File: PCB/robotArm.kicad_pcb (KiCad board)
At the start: 2 copper layers, 66 parts, among them J1 Motor_eje_X, J10 Gripper, J11 Conector Auxiliar 2, J12 5v, J13 End-Stop-X, J14 End-Stop-Y, J15 End-Stop-Z, J16 jumperLed5v, J17 Conector Auxiliar 1, J18 jumperLedVbat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

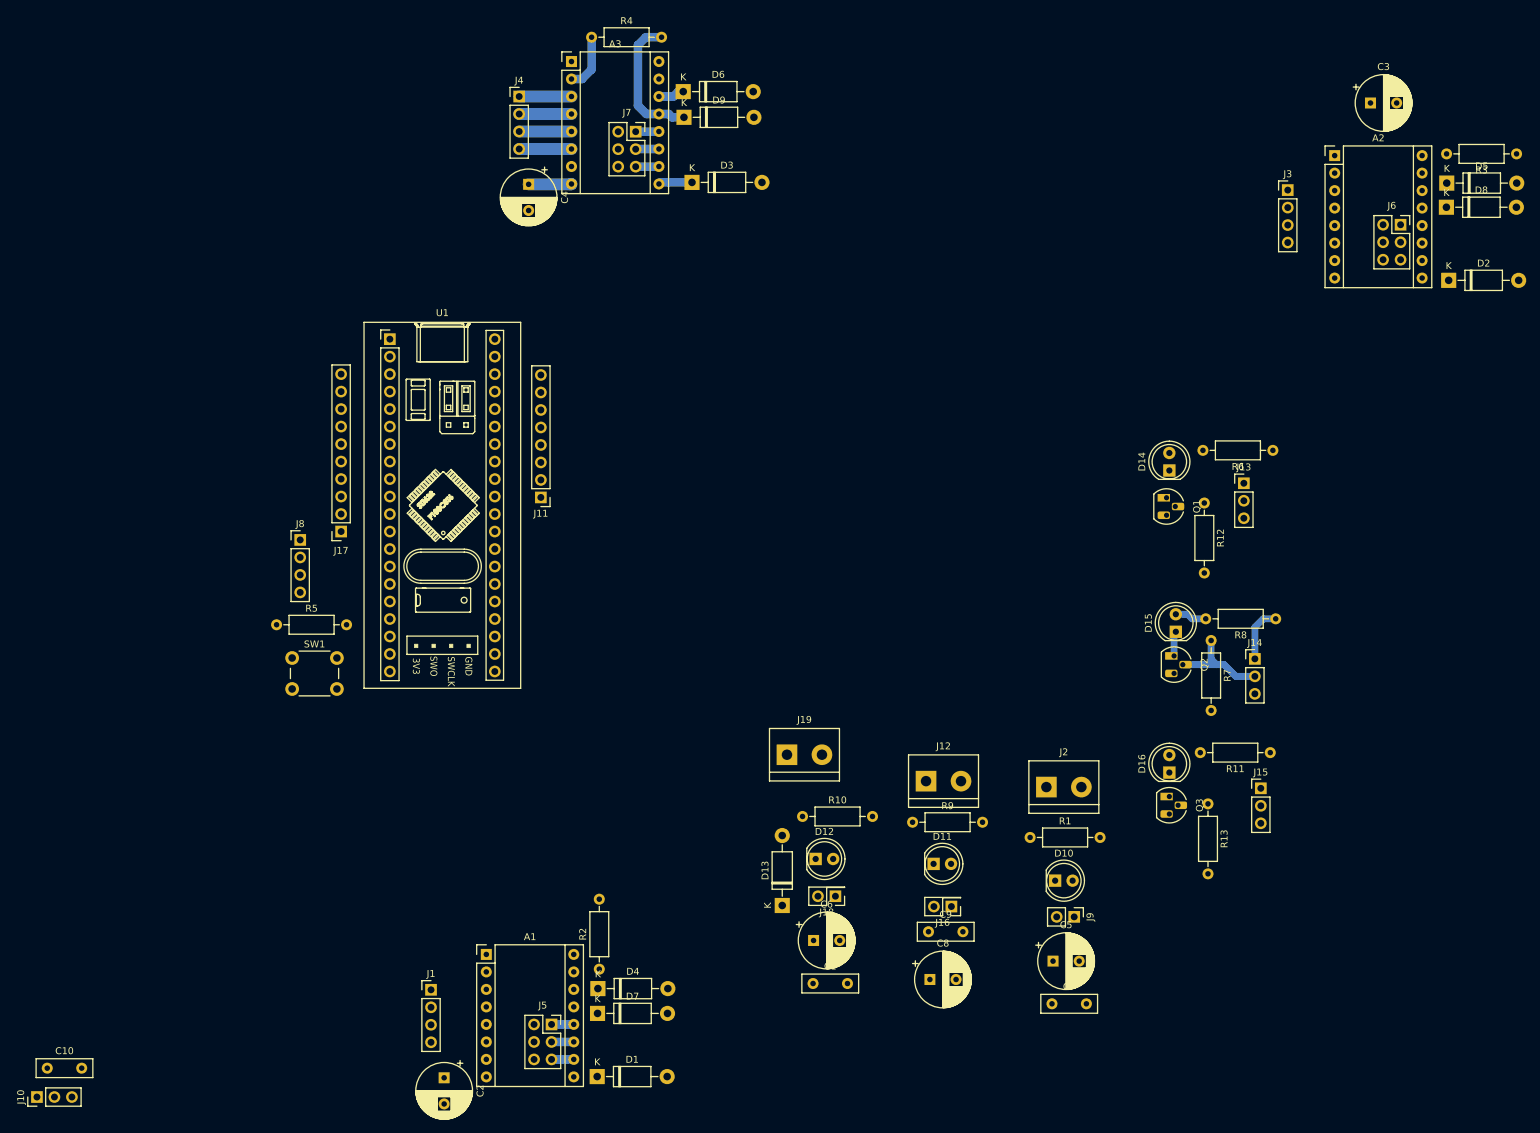
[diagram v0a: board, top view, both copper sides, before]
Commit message: Se avanzó con el diseño de la PCB, falta resolver Vin
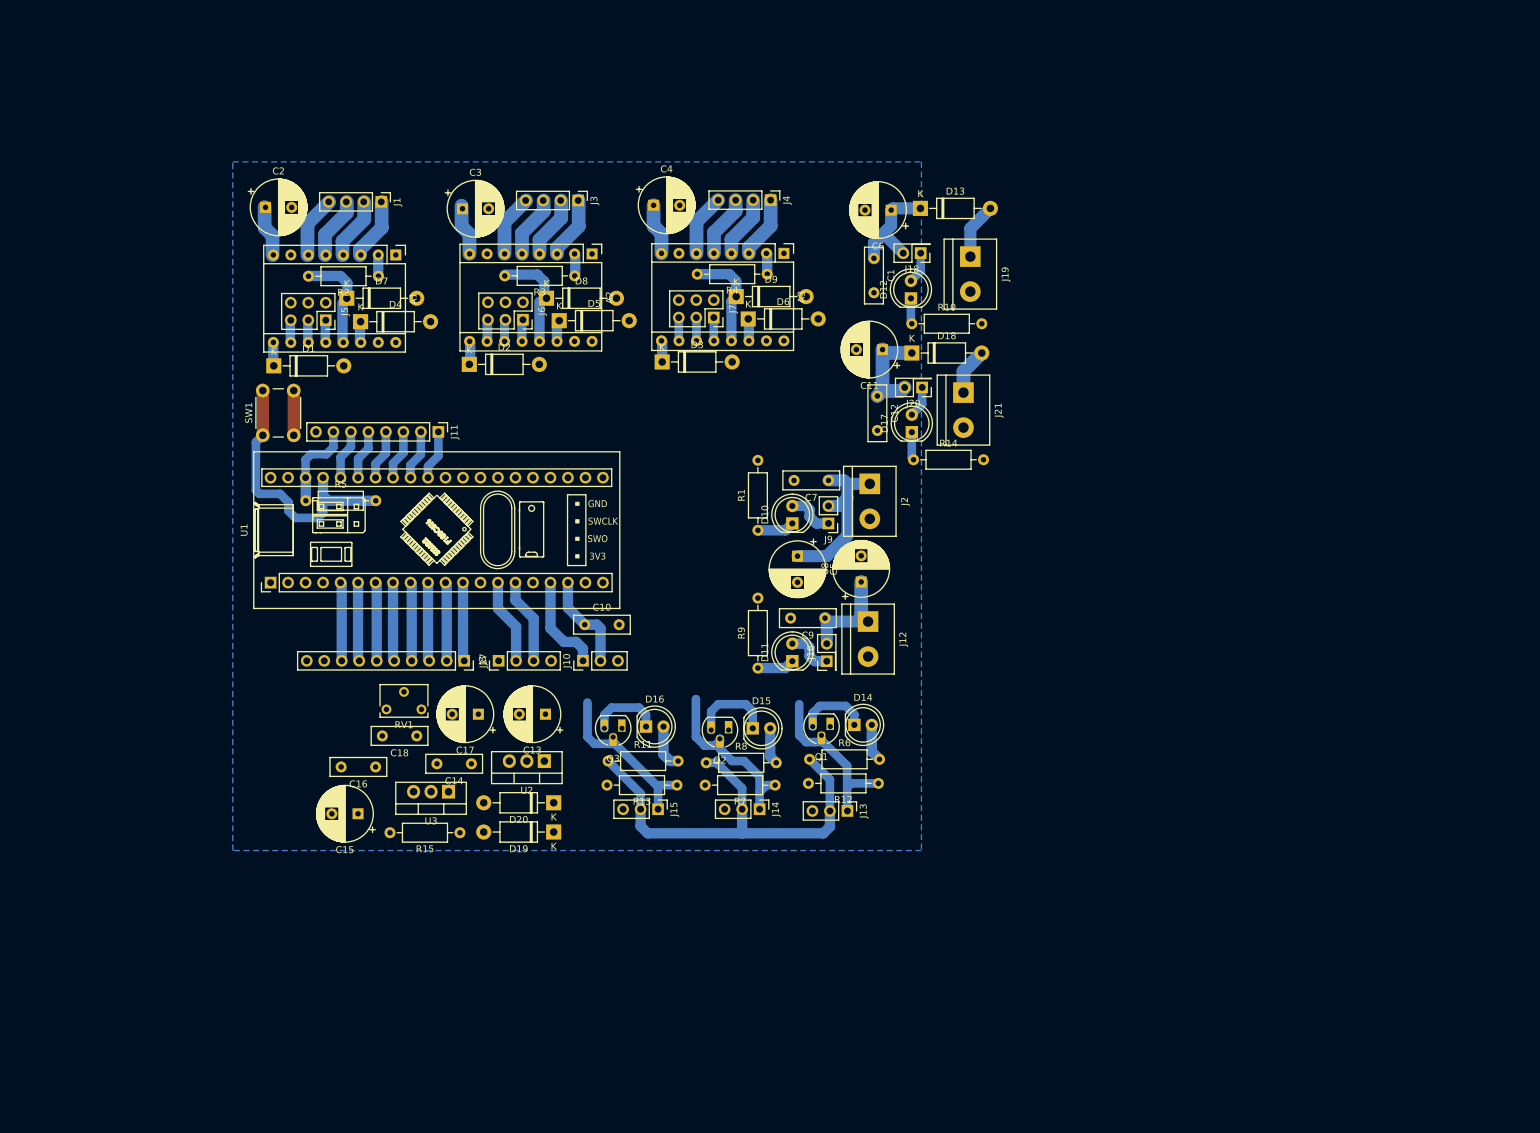
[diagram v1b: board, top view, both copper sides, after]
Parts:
- added C11: 470uF, Capacitor_THT:CP_Radial_D8.0mm_P3.80mm, F.Cu at (153.4, 76.7)
- added C12: 103, Capacitor_THT:C_Disc_D8.0mm_W2.5mm_P5.00mm, F.Cu at (152.7, 83.4)
- added C13: 470uF, Capacitor_THT:CP_Radial_D8.0mm_P3.80mm, F.Cu at (104.5, 129.6)
- added C14: 103, Capacitor_THT:C_Disc_D8.0mm_W2.5mm_P5.00mm, F.Cu at (93.7, 136.8)
- added C15: 220uF, Capacitor_THT:CP_Radial_D8.0mm_P3.80mm, F.Cu at (77.2, 144.1)
- added C16: 104, Capacitor_THT:C_Disc_D8.0mm_W2.5mm_P5.00mm, F.Cu at (79.8, 137.3)
- added C17: 100uF, Capacitor_THT:CP_Radial_D8.0mm_P3.80mm, F.Cu at (94.7, 129.6)
- added C18: 103, Capacitor_THT:C_Disc_D8.0mm_W2.5mm_P5.00mm, F.Cu at (85.8, 132.8)
- added D17: LED_Vcc, LED_THT:LED_D5.0mm, F.Cu at (157.7, 88.7)
- added D18: 1N4007, Diode_THT:D_DO-41_SOD81_P10.16mm_Horizontal, F.Cu at (157.7, 77.2)
- added D19: 1N4007, Diode_THT:D_DO-41_SOD81_P10.16mm_Horizontal, F.Cu at (105.6, 146.7)
- added D20: 1N4007, Diode_THT:D_DO-41_SOD81_P10.16mm_Horizontal, F.Cu at (105.6, 142.5)
- added J20: jumperLedVcc, Connector_PinHeader_2.54mm:PinHeader_2x01_P2.54mm_Vertical, F.Cu at (159.2, 82.2)
- added J21: Vcc, TerminalBlock:TerminalBlock_bornier-2_P5.08mm, F.Cu at (165.2, 82.9)
- added R14: 220, Resistor_THT:R_Axial_DIN0207_L6.3mm_D2.5mm_P10.16mm_Horizontal, F.Cu at (157.9, 92.7)
- added R15: 330, Resistor_THT:R_Axial_DIN0207_L6.3mm_D2.5mm_P10.16mm_Horizontal, F.Cu at (92.0, 146.8)
- added RV1: 1K, Potentiometer_THT:Potentiometer_Bourns_3266W_Vertical, F.Cu at (81.4, 128.9)
- added U2: LM7805_TO220, Package_TO_SOT_THT:TO-220-3_Vertical, F.Cu at (104.3, 136.4)
- added U3: LM317_TO-220, Package_TO_SOT_THT:TO-220-3_Vertical, F.Cu at (90.4, 140.9)
- Q1, Q2, Q3: value BC548 -> BC558
- moved D2 142.7 mm to (93.4, 78.8)
- moved R3 137.9 mm to (108.7, 66.0)
- moved C3 132.7 mm to (92.4, 56.2)
- moved D8 131.3 mm to (104.6, 69.2)
- moved D5 130.4 mm to (106.5, 72.5)
- moved C2 129.0 mm to (63.8, 56.0), turned to 0 degrees
- moved J6 128.2 mm to (101.2, 72.3), turned to 270 degrees
- moved J1 114.6 mm to (80.6, 55.2), turned to 270 degrees
- moved D1 113.4 mm to (65.0, 79.0)
- moved D7 110.0 mm to (75.6, 69.2)
- moved A2 108.8 mm to (111.2, 62.8), turned to 270 degrees
- moved J5 107.4 mm to (72.5, 72.4), turned to 270 degrees
- moved C6 106.7 mm to (154.7, 56.4), turned to 180 degrees
- moved C1 105.7 mm to (152.2, 63.4), turned to 270 degrees
- moved R2 105.6 mm to (80.2, 66.0), turned to 180 degrees
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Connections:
- J13 pad 1: +3V3 -> StopX
- J13 pad 2: StopX -> +3V3
- J14 pad 1: +3V3 -> StopY
- J14 pad 2: StopY -> +3V3
- J15 pad 1: +3V3 -> StopZ
- J15 pad 2: StopZ -> +3V3
- Q1 pad 1: Net-(D14-Pad1) -> GNDREF
- Q1 pad 3: GNDREF -> Net-(D14-Pad1)
- Q2 pad 1: Net-(D15-Pad1) -> GNDREF
- Q2 pad 3: GNDREF -> Net-(D15-Pad1)
- Q3 pad 1: Net-(D16-Pad1) -> GNDREF
- Q3 pad 3: GNDREF -> Net-(D16-Pad1)
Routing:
- net +3V3: track 16.3 -> 111.4 mm
- net Net-(R5-Pad2): track 0.00 -> 40.4 mm
- net VCC: track 6.24 -> 37.4 mm
- net +5V: track 0.00 -> 30.3 mm
- net StopX: track 0.00 -> 27.1 mm
- net StopZ: track 0.00 -> 25.6 mm
- net +BATT: track 0.00 -> 16.7 mm
- net Gripper: track 0.00 -> 14.3 mm
- net Net-(A2-Pad13): track 0.00 -> 14.1 mm
- net Net-(A1-Pad13): track 0.00 -> 14.1 mm
- net Net-(J8-Pad2): track 0.00 -> 12.4 mm
- net Net-(J8-Pad3): track 0.00 -> 12.4 mm
- net Net-(J17-Pad8): track 0.00 -> 11.4 mm
- net Net-(J17-Pad7): track 0.00 -> 11.4 mm
- net Net-(J17-Pad6): track 0.00 -> 11.4 mm
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- added copper zone on B.Cu, net GNDREF

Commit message: Se avanzó con el diseño de la PCB
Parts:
- moved C15 106.8 mm to (146.0, 62.4), turned to 0 degrees
- moved C14 97.4 mm to (154.8, 61.0), turned to 270 degrees
- moved C16 93.0 mm to (147.6, 73.6), turned to 90 degrees
- moved D19 90.5 mm to (151.0, 68.4), turned to 270 degrees
- moved C13 88.1 mm to (153.4, 56.4), turned to 90 degrees
- moved RV1 83.8 mm to (152.0, 83.8)
- moved U3 83.2 mm to (155.0, 88.4), turned to 270 degrees
- moved U2 82.8 mm to (154.8, 70.8), turned to 270 degrees
- moved R15 77.9 mm to (151.6, 96.6), turned to 90 degrees
- moved D20 76.2 mm to (147.8, 79.0), turned to 270 degrees
- moved C18 72.8 mm to (151.4, 101.2)
- moved C17 62.4 mm to (145.4, 93.2), turned to 270 degrees
- moved R13 51.4 mm to (72.2, 139.2)
- moved J2 50.8 mm to (135.1, 144.2), turned to 180 degrees
- moved C1 50.6 mm to (139.6, 112.4)
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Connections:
- J17 pad 1: Net-(J17-Pad1) -> +3V3
- J17 pad 9: +3V3 -> Net-(J17-Pad9)
- U1 pad 10: Net-(J17-Pad3) -> Net-(J17-Pad4)
- U1 pad 11: Net-(J17-Pad2) -> Net-(J17-Pad3)
- U1 pad 12: Net-(J17-Pad1) -> Net-(J17-Pad2)
- U1 pad 5: Net-(J17-Pad8) -> Net-(J17-Pad9)
- U1 pad 6: Net-(J17-Pad7) -> Net-(J17-Pad8)
- U1 pad 7: Net-(J17-Pad6) -> Net-(J17-Pad7)
- U1 pad 8: Net-(J17-Pad5) -> Net-(J17-Pad6)
- U1 pad 9: Net-(J17-Pad4) -> Net-(J17-Pad5)
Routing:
- net +3V3: track 111.4 -> 185.1 mm, vias 0 -> 4
- net +5V: track 30.3 -> 96.6 mm
- net StopX: track 27.1 -> 65.6 mm
- net StopY: track 26.4 -> 53.4 mm
- net VCC: track 37.4 -> 57.1 mm
- net StopZ: track 25.6 -> 42.5 mm
- net Net-(J17-Pad1): track 11.4 -> 0.00 mm
- net GNDREF: track 6.50 -> 16.1 mm, vias 0 -> 4
- net Net-(J17-Pad9): track 0.00 -> 9.44 mm
- net Net-(D15-Pad1): track 12.1 -> 4.48 mm
- net Net-(D16-Pad1): track 10.6 -> 4.44 mm
- net Net-(D14-Pad1): track 10.4 -> 4.39 mm
- net Net-(D10-Pad1): track 5.41 -> 10.6 mm
- net Net-(J8-Pad2): track 12.4 -> 8.18 mm
- net Net-(J8-Pad3): track 12.4 -> 8.18 mm
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
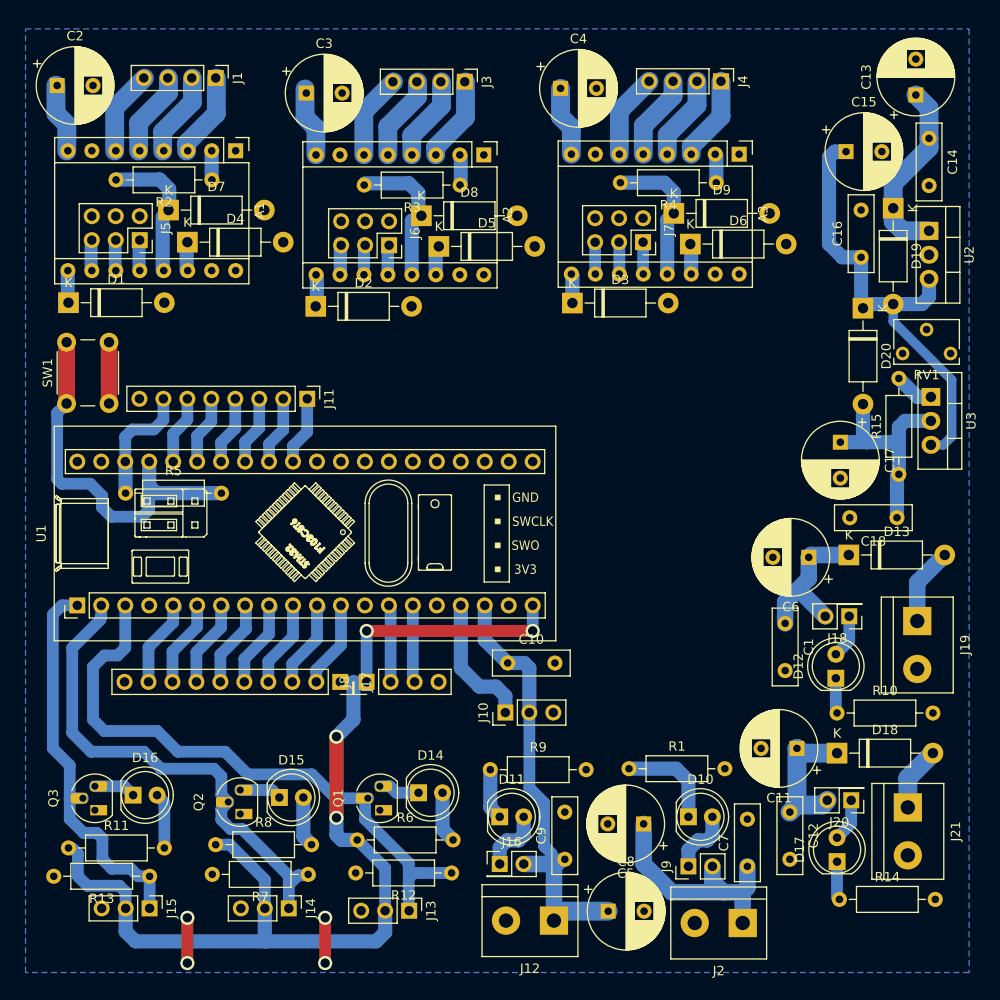
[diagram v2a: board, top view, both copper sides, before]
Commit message: Se logró conectar todos lso dispositivos en la PCB
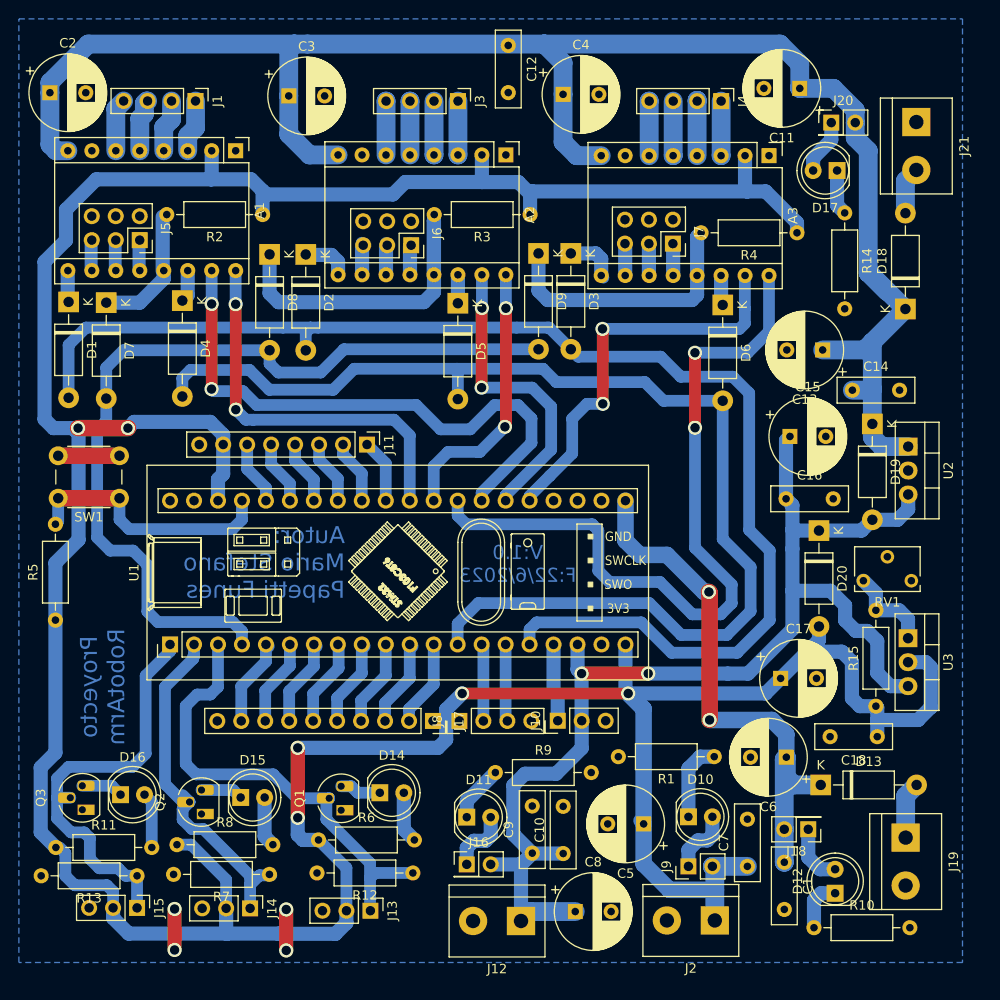
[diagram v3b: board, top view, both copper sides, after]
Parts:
- moved C12 86.6 mm to (110.2, 51.2)
- moved D17 73.2 mm to (145.1, 64.4), turned to 180 degrees
- moved R14 72.8 mm to (145.9, 68.9), turned to 270 degrees
- moved J21 72.6 mm to (153.5, 59.3)
- moved J20 71.9 mm to (144.4, 59.3), turned to 0 degrees
- moved C11 69.9 mm to (141.1, 55.7)
- moved D18 47.6 mm to (152.3, 79.1), turned to 90 degrees
- moved C15 30.8 mm to (140.1, 92.6)
- moved C13 28.8 mm to (143.5, 83.4), turned to 180 degrees
- moved C14 27.9 mm to (146.7, 87.7), turned to 0 degrees
- moved C16 26.8 mm to (139.6, 99.2), turned to 0 degrees
- moved C17 25.8 mm to (139.1, 118.2), turned to 0 degrees
- moved U3 25.7 mm to (152.6, 114.0)
- moved C1 25.3 mm to (139.5, 137.7)
- moved R15 24.7 mm to (149.2, 121.2)
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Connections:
- J21 pad 1: Net-(D18-Pad2) -> GNDREF
- J21 pad 2: GNDREF -> Net-(D18-Pad2)
- U1 pad 25: StepX -> StepZ
- U1 pad 27: StepZ -> StepX
- U1 pad 28: DirX -> DirZ
- U1 pad 30: DirZ -> DirX
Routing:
- net +3V3: track 185.1 -> 411.1 mm, vias 4 -> 6
- net EnableMotor: track 0.00 -> 139.1 mm
- net VCC: track 57.1 -> 185.4 mm
- net SleepMotor: track 0.00 -> 126.1 mm
- net ResetMotor: track 0.00 -> 91.6 mm
- net DirZ: track 0.00 -> 80.8 mm, vias 0 -> 2
- net StepX: track 0.00 -> 60.8 mm, vias 0 -> 2
- net StepZ: track 0.00 -> 42.9 mm, vias 0 -> 2
- net DirX: track 0.00 -> 41.2 mm, vias 0 -> 2
- net +BATT: track 16.7 -> 57.5 mm, vias 0 -> 2
- net +5V: track 96.6 -> 130.7 mm, vias 0 -> 2
- net StepY: track 0.00 -> 32.2 mm, vias 0 -> 2
- net DirY: track 0.00 -> 29.1 mm, vias 0 -> 2
- net Net-(A2-Pad13): track 14.1 -> 35.7 mm
- net StopX: track 65.6 -> 50.3 mm
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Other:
- board text added: "Autor: Mario Stefano Papetti Funes"
- board text added: "Proyecto RobotArm"
- board text added: "V:1.0 F:22/6/2023"
